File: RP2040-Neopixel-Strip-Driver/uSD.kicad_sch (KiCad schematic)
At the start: 1 part

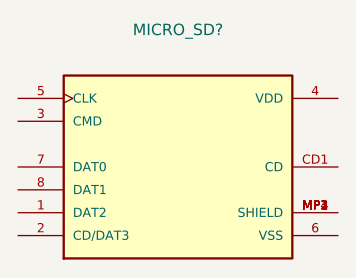
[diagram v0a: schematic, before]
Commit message: Made microphone symbol, footprint, and 3D model.
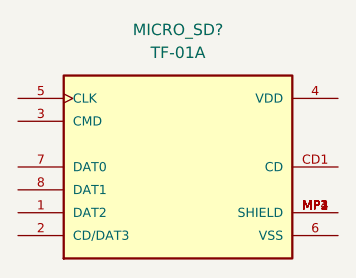
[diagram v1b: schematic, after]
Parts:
- MICRO_SD?: value (none) -> TF-01A; footprint (none) -> TF-01A
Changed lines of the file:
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@@
     (in_bom yes) (on_board yes) (fields_autoplaced)
     (property "Reference" "MICRO_SD?" (id 0) (at 151.13 74.93 0))
-    (property "Value" "" (id 1) (at 151.13 77.47 0))
-    (property "Footprint" "" (id 2) (at 151.13 90.17 0)
+    (property "Value" "TF-01A" (id 1) (at 151.13 77.47 0))
+    (property "Footprint" "TF-01A" (id 2) (at 151.13 90.17 0)
       (effects (font (size 1.27 1.27)) (justify left bottom) hide)
     )
